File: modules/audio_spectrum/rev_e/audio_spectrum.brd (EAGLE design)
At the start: 68.1 x 66 mm, 111 parts, among them J1 AUDIO-JACK-VERTICAL, J2 MODULE_GENERIC_DEBUG, J3 TC2030-JLINK-L, P1 4k-200k, P2 4k-200k, Q1 NX3008PBK, Q2 NX3008PBK, U1 AT45DB641EUDFN, U10 TLV62130, U2 MP23AB02B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

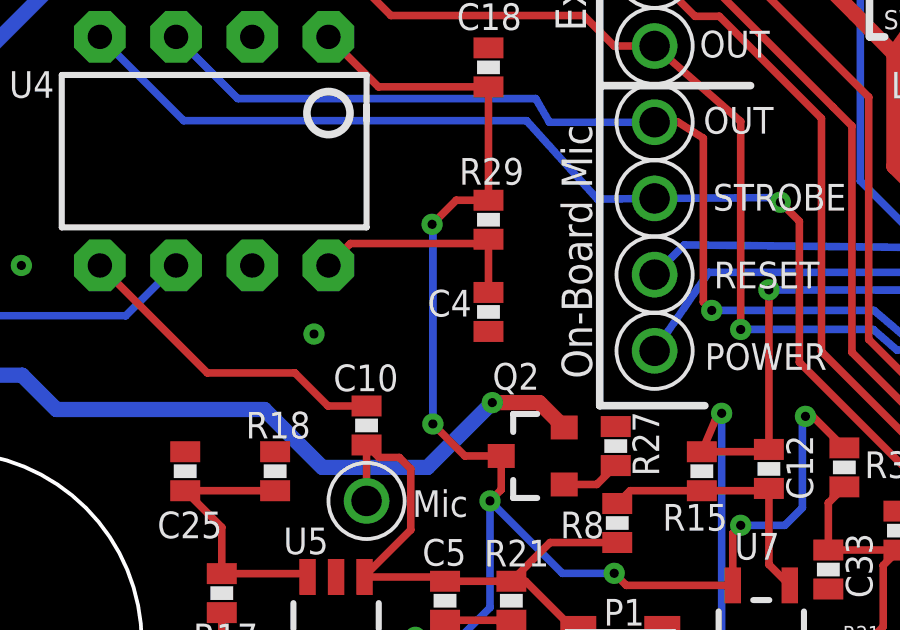
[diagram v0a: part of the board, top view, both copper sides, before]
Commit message: fixed spec reset airwire
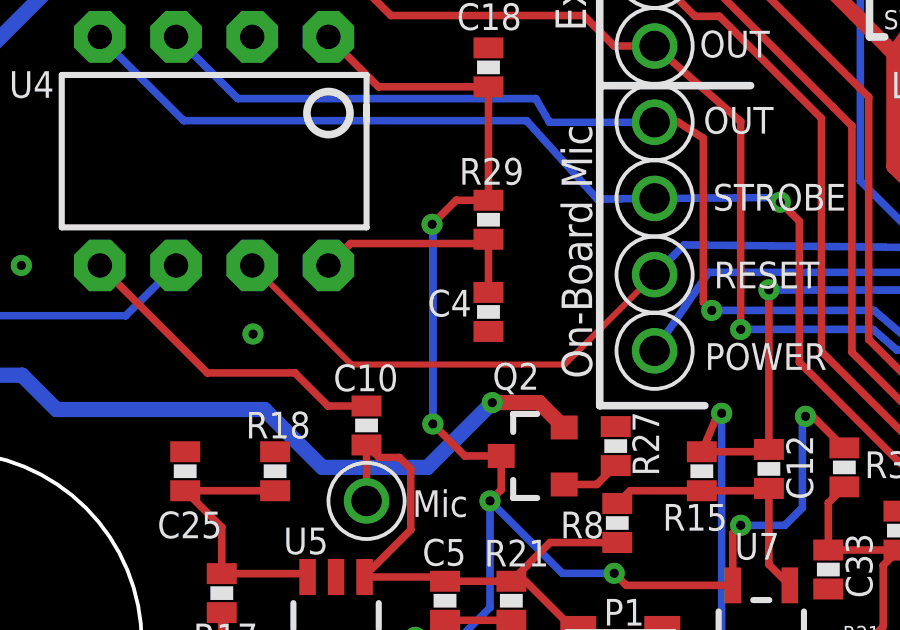
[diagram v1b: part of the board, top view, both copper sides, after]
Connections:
- removed net N$22: TP7.TESTPOINT, U9.11
- net SPEC_RESET: now also TP7.TESTPOINT, U9.11
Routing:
- net SPEC_RESET: track 0.00 -> 36.2 mm, vias 0 -> 1
- net N$22: track 20.2 -> 0.00 mm, vias 1 -> 0
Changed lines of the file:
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@@
 <via x="23.0632" y="39.7764" extent="1-16" drill="0.3048"/>
 <via x="7.7978" y="27.178" extent="1-16" drill="0.3048"/>
-<via x="17.5514" y="24.892" extent="1-16" drill="0.3048"/>
+<via x="15.5194" y="24.892" extent="1-16" drill="0.3048"/>
 <via x="40.005" y="51.181" extent="1-16" drill="0.3048"/>
 <via x="37.4904" y="41.5036" extent="1-16" drill="0.3048"/>
@@
 <signal name="SPEC_RESET">
 <contactref element="U4" pad="7"/>
+<contactref element="TP7" pad="TESTPOINT"/>
+<contactref element="U9" pad="11"/>
+<via x="43.4848" y="27.7114" extent="1-16" drill="0.3048"/>
+<wire x1="43.4848" y1="27.7114" x2="29.8958" y2="27.8638" width="0.254" layer="16"/>
+<wire x1="29.8958" y1="27.8638" x2="28.9052" y2="26.8732" width="0.254" layer="16"/>
+<wire x1="48.6118" y1="27.8838" x2="43.6572" y2="27.8838" width="0.254" layer="1"/>
+<wire x1="43.6572" y1="27.8838" x2="43.4848" y2="27.7114" width="0.254" layer="1"/>
+<wire x1="28.9052" y1="26.8732" x2="25.908" y2="23.876" width="0.2032" layer="1"/>
+<wire x1="18.796" y1="23.876" x2="15.494" y2="27.178" width="0.2032" layer="1"/>
+<wire x1="25.908" y1="23.876" x2="18.796" y2="23.876" width="0.2032" layer="1"/>
 </signal>
 <signal name="SPEC_GATED">
@@
 <wire x1="30.988" y1="52.0192" x2="31.6531" y2="51.3541" width="0.254" layer="1"/>
 </signal>
-<signal name="N$22">
-<contactref element="TP7" pad="TESTPOINT"/>
-<contactref element="U9" pad="11"/>
-<via x="43.4848" y="27.7114" extent="1-16" drill="0.3048"/>
-<wire x1="43.4848" y1="27.7114" x2="29.8958" y2="27.8638" width="0.254" layer="16"/>
-<wire x1="29.8958" y1="27.8638" x2="28.9052" y2="26.8732" width="0.254" layer="16"/>
-<wire x1="48.6118" y1="27.8838" x2="43.6572" y2="27.8838" width="0.254" layer="1"/>
-<wire x1="43.6572" y1="27.8838" x2="43.4848" y2="27.7114" width="0.254" layer="1"/>
-</signal>
 <signal name="N$24">

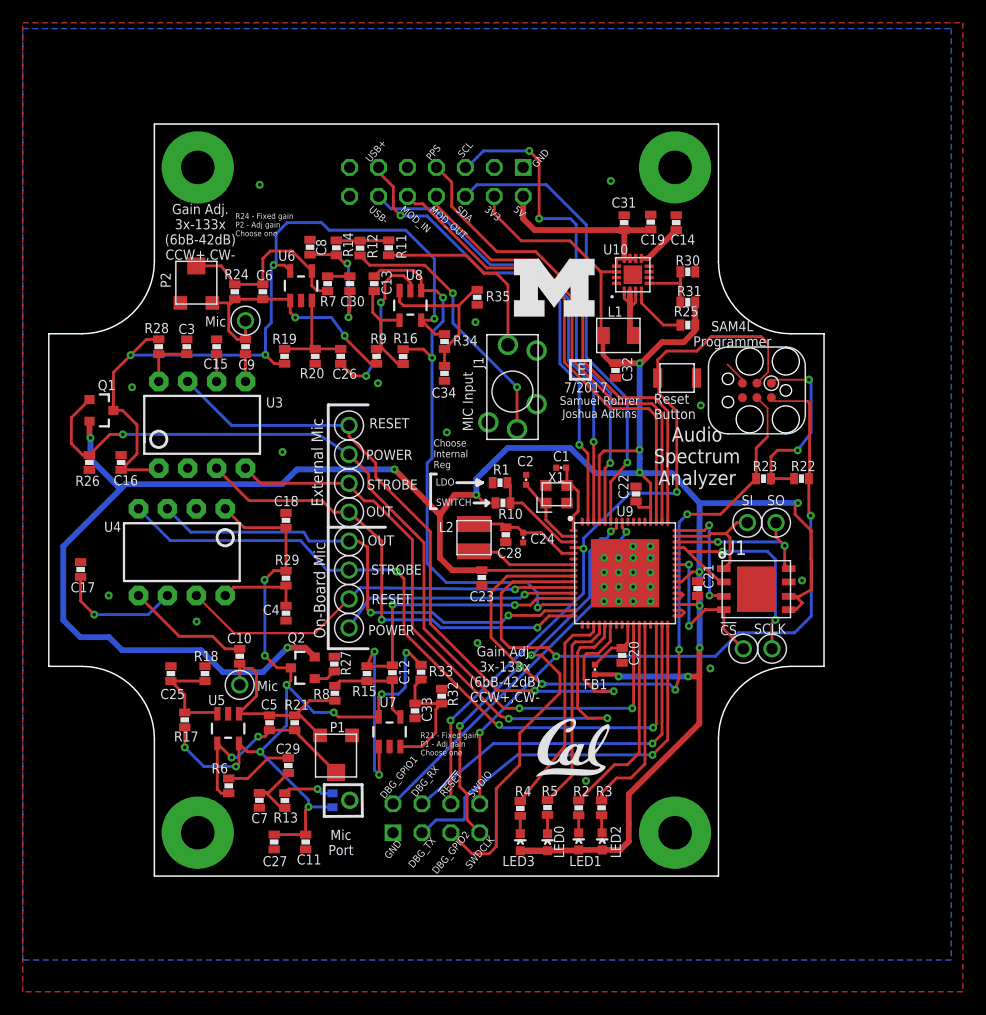
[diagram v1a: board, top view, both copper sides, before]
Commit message: changed to design block for header parts
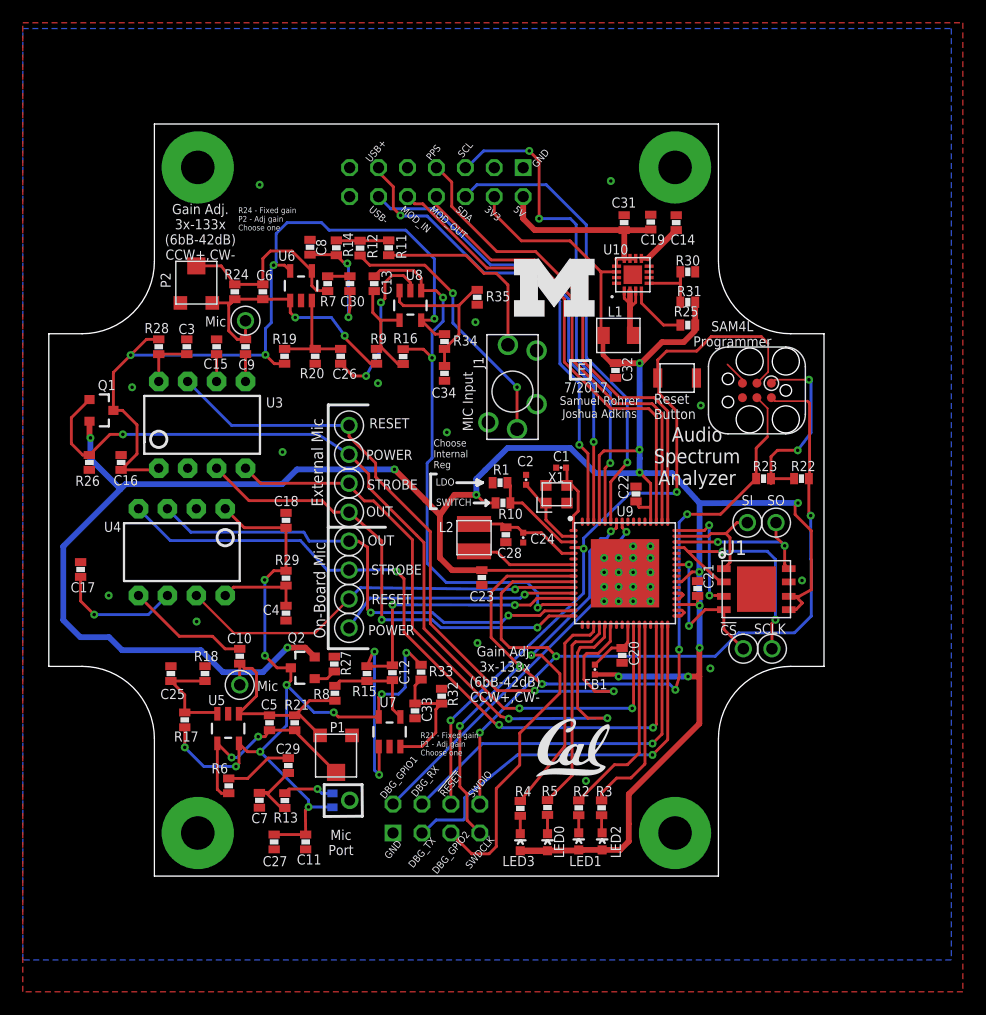
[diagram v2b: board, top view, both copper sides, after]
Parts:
- removed J2: MODULE_GENERIC_DEBUG, signpost:MODULE_GENERIC_DEBUG
- added J6: SIGNPOST_MODULE_HEADER, signpost:SIGNPOST_MODULE_HEADER
- added J7: SIGNPOST_DEBUG_HEADER, signpost:SIGNPOST_DEBUG_HEADER
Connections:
- net !AUDIO_RESET: now also J7.20; no longer J2.20
- net 3V3: now also J6.4; no longer J2.4
- net 5V: now also J6.2; no longer J2.2
- net AUDIO_SWDCLK: now also J7.21; no longer J2.21
- net AUDIO_SWDIO: now also J7.22; no longer J2.22
- net DBG_GPIO1: now also J7.16; no longer J2.16
- net DBG_GPIO2: now also J7.19; no longer J2.19
- net DBG_RX: now also J7.18; no longer J2.18
- net DBG_TX: now also J7.17; no longer J2.17
- net GND: now also J6.1, J6.14, J7.15; no longer J2.1, J2.14, J2.15
- net MOD_IN: now also J6.10; no longer J2.10
- net MOD_OUT: now also J6.8; no longer J2.8
- net PPS: now also J6.7; no longer J2.7
- net SCL: now also J6.5; no longer J2.5
- net SDA: now also J6.6; no longer J2.6
- net USB+: now also J6.11; no longer J2.11
- net USB-: now also J6.12; no longer J2.12
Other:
- board text added: "0.1 / 2.54 Above PCB"
- board text added: "0.358 / 9.10 Below PCB"
- board text added: "Drill 0.116 @ (-0.825, -1.15)"
- board text added: "Drill 0.116 @ (-0.825, 1.15)"
- board text added: "Drill 0.116 @ (0.825, -1.15)"
- board text added: "Drill 0.116 @ (0.825, 1.15)"

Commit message: renumbered parts
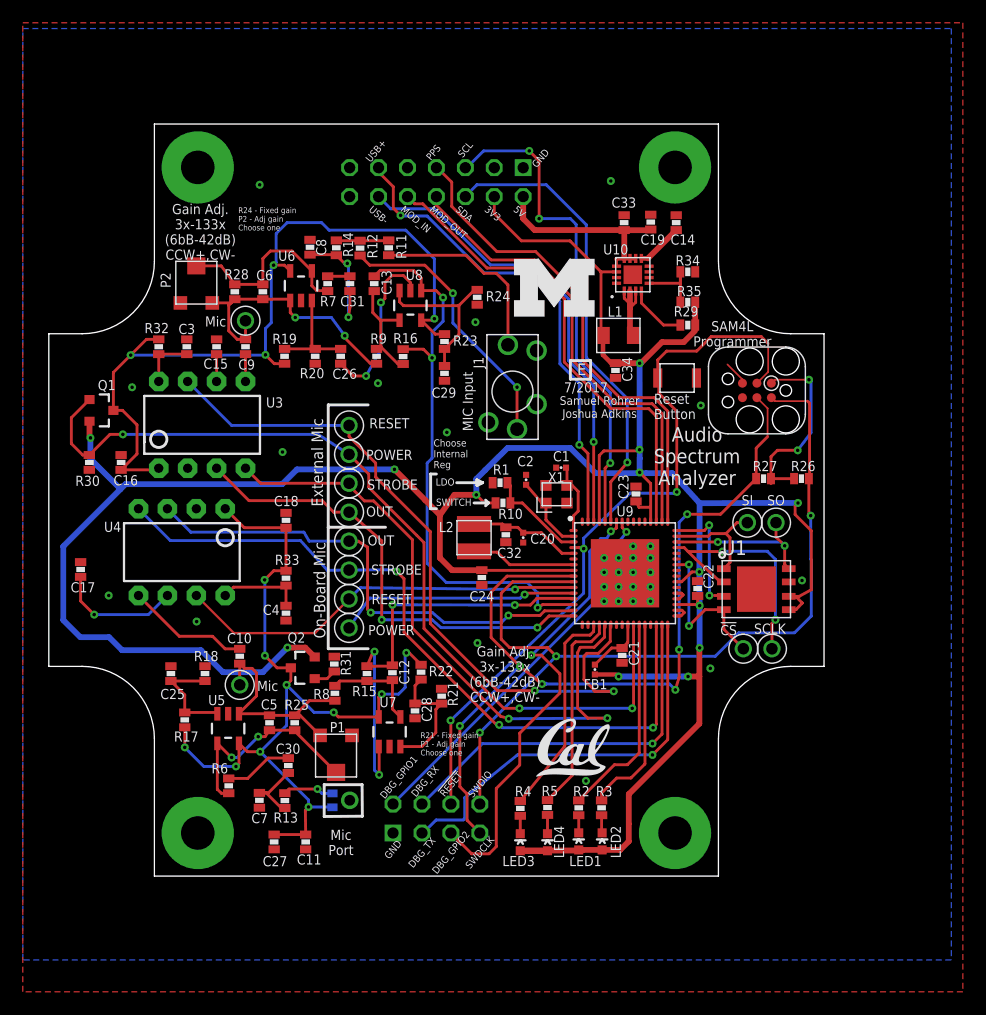
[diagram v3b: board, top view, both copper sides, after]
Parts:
- removed J6: SIGNPOST_MODULE_HEADER, signpost:SIGNPOST_MODULE_HEADER
- added J4: TC2030-JLINK-L, connector:TC2030-IDC
- C20: device passives:0603_CAP -> passives:0402_CAP
- C24: device passives:0402_CAP -> passives:0603_CAP
- C28: value 6.8uF -> 1uF
- C29: value 4.7uF -> 1uF
- C31: value 10uF -> 4.7uF
- C32: value 22uF -> 6.8uF
- C33: value 1uF -> 10uF
- C34: value 1uF -> 22uF
- J3: value TC2030-JLINK-L -> SIGNPOST_MODULE_HEADER; device connector:TC2030-IDC -> signpost:SIGNPOST_MODULE_HEADER
- R21: value 60k -> 20k
- R22, R23, R24: value 100k -> 20k
- R25: value 100k -> 60k
- R28, R29: value 200k -> 100k
- R30: value 240k -> 100k
- R31: value 750k -> 100k
- R32, R33: value 20k -> 200k
- R34: value 20k -> 240k
- R35: value 20k -> 750k
- moved R26 62.6 mm to (68.6, 37.4), turned to 180 degrees
- moved R30 55.2 mm to (6.10, 38.9), turned to 270 degrees
- moved R25 49.1 mm to (24.1, 16.0), turned to 90 degrees
- moved C33 46.6 mm to (53.1, 59.9)
- moved R31 44.4 mm to (27.6, 21.2), turned to 90 degrees
- moved C30 42.7 mm to (23.6, 12.2)
- moved R29 41.7 mm to (58.6, 50.9), turned to 0 degrees
- moved R27 41.1 mm to (65.3, 37.4), turned to 0 degrees
- moved R32 39.5 mm to (12.2, 49.0), turned to 270 degrees
- moved R22 37.5 mm to (35.2, 20.4), turned to 270 degrees
- moved C29 37.1 mm to (37.3, 46.7), turned to 90 degrees
- moved J3 33.6 mm to (36.6, 63.5), turned to 0 degrees
- moved R23 30.5 mm to (37.3, 49.5), turned to 270 degrees
- moved C31 24.7 mm to (29.0, 54.6), turned to 270 degrees
- moved R34 22.2 mm to (58.6, 55.6), turned to 180 degrees
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- renumbered J7 to J2, LED0 to LED4
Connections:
- net !AUDIO_RESET: now also J4.3; no longer J3.3
- net 3V3: now also C24.1, C34.2, J3.4, J4.1, R26.2, R27.2, R29.2, R35.2; no longer C21.1, C32.2, J3.1, J6.4, R22.2, R23.2, R25.2, R31.2
- net 5V: now also C33.1, J3.2; no longer C31.1, J6.2
- net AUDIO_SWDCLK: now also J4.4, R27.1; no longer J3.4, R23.1
- net AUDIO_SWDIO: now also J4.2, R26.1; no longer J3.2, R22.1
- net GND: now also C28.1, C29.1, C32.2, C33.2, J3.1, J3.14, J4.5, R21.2, R24.2, R30.2, R31.2, R34.1; no longer C28.2, C31.2, C32.1, C33.1, J3.5, J6.1, J6.14, R26.2, R27.2, R30.1, R32.2, R35.2
- net MOD_IN: now also J3.10; no longer J6.10
- net MOD_OUT: now also J3.8; no longer J6.8
- net N$12: now also R25.1; no longer R21.1
- net N$13: now also C30.1; no longer C29.1
- net N$14: now also R28.1; no longer R24.1
- net N$15: now also C31.1; no longer C30.1
- net N$2: now also R32.2; no longer R28.2
- net N$20: now also C31.2; no longer C30.2
- net N$27: now also C28.2, R21.1, R22.2; no longer C33.2, R32.1, R33.2
- net N$28: now also C29.2, R23.2, R24.1; no longer C34.2, R34.2, R35.1
- net N$29: now also C20.1, C32.1; no longer C24.1, C28.1
- net N$32: now also C21.1; no longer C20.1
- net N$36: now also R29.1; no longer R25.1
- net N$37: now also R34.2, R35.1; no longer R30.2, R31.1
- net N$5: now also C30.2; no longer C29.2
- net N$6: now also R33.2; no longer R29.2
- net N87: now also R28.2; no longer R24.2
- net N90: now also R25.2; no longer R21.2
- net PPS: now also J3.7; no longer J6.7
- net SCL: now also J3.5; no longer J6.5
- net SDA: now also J3.6; no longer J6.6
- net SPEC2_GATED: now also R23.1, R32.1; no longer R28.1, R34.1
- net SPEC2_POWER: now also R30.1; no longer R26.1
- net SPEC_GATED: now also R22.1; no longer R29.1
- net SPEC_POWER: now also R31.1; no longer R27.1
- net USB+: now also J3.11; no longer J6.11
- net USB-: now also J3.12; no longer J6.12

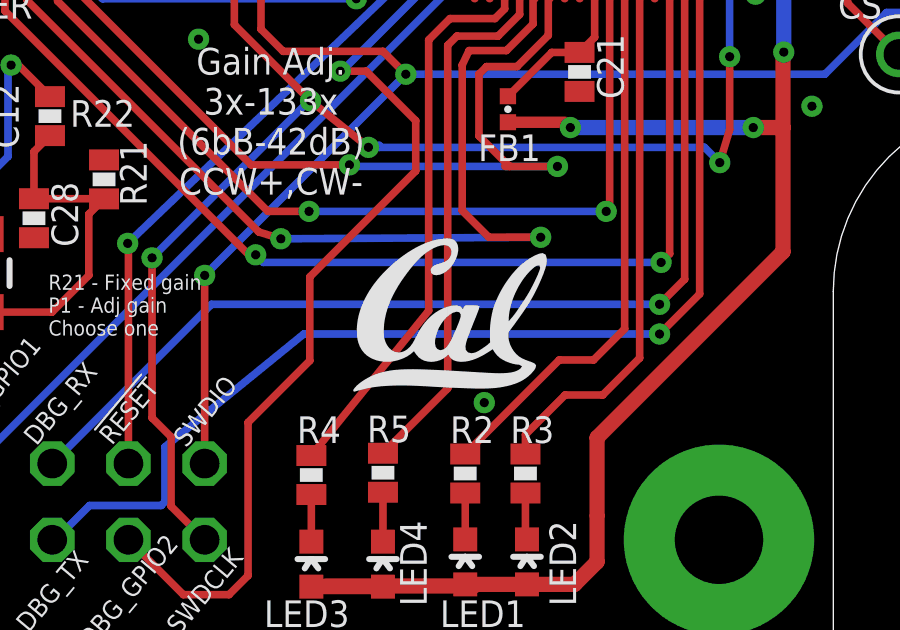
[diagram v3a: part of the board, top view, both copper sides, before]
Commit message: added MPN, new BOM
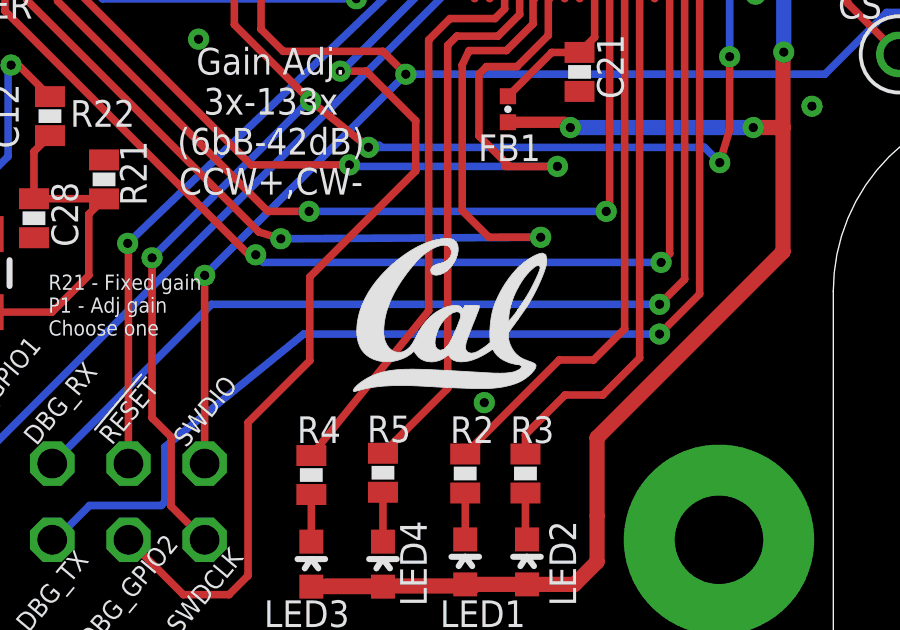
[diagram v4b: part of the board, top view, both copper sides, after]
